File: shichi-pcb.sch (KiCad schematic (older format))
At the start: 34 parts, among them J1 USB_C_Receptacle_HRO_TYPE-C-3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, J2 Conn_01x04_Male, J3 Conn_01x06_Male, J4 Conn_01x04_Male, J5 Conn_01x02_Male, J6 Conn_01x01_Male, SW1 SW_Push, SW2 SW_Push, U1 MCP1700-3302E_SOT23, U2 USBLC6-2SC6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

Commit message: Remove USB headers
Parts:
- removed J2: Conn_01x04_Male, Connector_PinSocket_2.54mm:PinSocket_1x04_P2.54mm_Vertical, symbol Connector:Conn_01x04_Male
- renumbered J3 to J2, J4 to J3, J5 to J4, J6 to J5
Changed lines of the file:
@@
 EESchema Schematic File Version 4
 LIBS:shichi-pcb-cache
-EELAYER 29 0
+EELAYER 30 0
 EELAYER END
 $Descr A4 11693 8268
@@
 NRST
 $Comp
-L power:VCC #PWR04
+L power:VCC #PWR02
 U 1 1 5CFA87A5
 P 2350 4950
-F 0 "#PWR04" H 2350 4800 50  0001 C CNN
+F 0 "#PWR02" H 2350 4800 50  0001 C CNN
 F 1 "VCC" H 2367 5123 50  0000 C CNN
 F 2 "" H 2350 4950 50  0001 C CNN
@@
 $EndComp
 $Comp
-L power:GND #PWR011
+L power:GND #PWR09
 U 1 1 5CFB408D
 P 4300 3250
-F 0 "#PWR011" H 4300 3000 50  0001 C CNN
+F 0 "#PWR09" H 4300 3000 50  0001 C CNN
 F 1 "GND" H 4305 3077 50  0000 C CNN
 F 2 "" H 4300 3250 50  0001 C CNN
@@
 $EndComp
 $Comp
-L power:GND #PWR020
+L power:GND #PWR018
 U 1 1 5CFB6455
 P 7300 1700
-F 0 "#PWR020" H 7300 1450 50  0001 C CNN
+F 0 "#PWR018" H 7300 1450 50  0001 C CNN
 F 1 "GND" H 7305 1527 50  0000 C CNN
 F 2 "" H 7300 1700 50  0001 C CNN
@@
 $EndComp
 $Comp
-L power:GND #PWR027
+L power:GND #PWR025
 U 1 1 5CFB6809
 P 10500 1600
-F 0 "#PWR027" H 10500 1350 50  0001 C CNN
+F 0 "#PWR025" H 10500 1350 50  0001 C CNN
 F 1 "GND" H 10505 1427 50  0000 C CNN
 F 2 "" H 10500 1600 50  0001 C CNN
@@
 	0    -1   -1   0
 $EndComp
-$Comp
-L power:GND #PWR03
-U 1 1 5CFB0CA6
-P 1450 7400
-F 0 "#PWR03" H 1450 7150 50  0001 C CNN
-F 1 "GND" H 1455 7227 50  0000 C CNN
-F 2 "" H 1450 7400 50  0001 C CNN
-F 3 "" H 1450 7400 50  0001 C CNN
-	1    1450 7400
-	0    -1   -1   0
-$EndComp
 Text GLabel 10500 2100 2    50   Input ~ 0
 SCL
@@
 SDA
 $Comp
-L power:GND #PWR029
+L power:GND #PWR027
 U 1 1 5D01D767
 P 10500 2400
-F 0 "#PWR029" H 10500 2150 50  0001 C CNN
+F 0 "#PWR027" H 10500 2150 50  0001 C CNN
 F 1 "GND" H 10505 2227 50  0000 C CNN
 F 2 "" H 10500 2400 50  0001 C CNN
@@
 Wire Wire Line
 	2750 4950 2950 4950
-$Comp
-L power:VCC #PWR02
-U 1 1 5D05176C
-P 1450 7100
-F 0 "#PWR02" H 1450 6950 50  0001 C CNN
-F 1 "VCC" H 1467 7273 50  0000 C CNN
-F 2 "" H 1450 7100 50  0001 C CNN
-F 3 "" H 1450 7100 50  0001 C CNN
-	1    1450 7100
-	0    1    1    0
-$EndComp
 Text GLabel 1950 5550 2    50   Input ~ 0
 D-Bus
@@
 	2200 5150 2350 5150
 $Comp
-L power:GND #PWR05
+L power:GND #PWR03
 U 1 1 5CFAFCDE
 P 2350 5300
-F 0 "#PWR05" H 2350 5050 50  0001 C CNN
+F 0 "#PWR03" H 2350 5050 50  0001 C CNN
 F 1 "GND" H 2355 5127 50  0000 C CNN
 F 2 "" H 2350 5300 50  0001 C CNN
@@
 	4500 6500 4550 6500
 $Comp
-L power:GND #PWR014
+L power:GND #PWR012
 U 1 1 5D32B978
 P 4550 6550
-F 0 "#PWR014" H 4550 6300 50  0001 C CNN
+F 0 "#PWR012" H 4550 6300 50  0001 C CNN
 F 1 "GND" H 4555 6377 50  0000 C CNN
 F 2 "" H 4550 6550 50  0001 C CNN
@@
 	3450 6500 3500 6500
 $Comp
-L power:VCC #PWR08
+L power:VCC #PWR06
 U 1 1 5D31D96D
 P 3450 6450
-F 0 "#PWR08" H 3450 6300 50  0001 C CNN
+F 0 "#PWR06" H 3450 6300 50  0001 C CNN
 F 1 "VCC" H 3467 6623 50  0000 C CNN
 F 2 "" H 3450 6450 50  0001 C CNN
@@
 	4450 5050 4450 5150
 $Comp
-L power:+3.3V #PWR013
+L power:+3.3V #PWR011
 U 1 1 5D1ECA69
 P 4450 4950
-F 0 "#PWR013" H 4450 4800 50  0001 C CNN
+F 0 "#PWR011" H 4450 4800 50  0001 C CNN
 F 1 "+3.3V" H 4465 5123 50  0000 C CNN
 F 2 "" H 4450 4950 50  0001 C CNN
@@
 Connection ~ 4450 5050
 $Comp
-L power:GND #PWR010
+L power:GND #PWR08
 U 1 1 5D1FE5B6
 P 4000 5550
-F 0 "#PWR010" H 4000 5300 50  0001 C CNN
+F 0 "#PWR08" H 4000 5300 50  0001 C CNN
 F 1 "GND" H 4005 5377 50  0000 C CNN
 F 2 "" H 4000 5550 50  0001 C CNN
@@
 $EndComp
 $Comp
-L power:GND #PWR07
+L power:GND #PWR05
 U 1 1 5D281CF4
 P 3350 4050
-F 0 "#PWR07" H 3350 3800 50  0001 C CNN
+F 0 "#PWR05" H 3350 3800 50  0001 C CNN
 F 1 "GND" H 3355 3877 50  0000 C CNN
 F 2 "" H 3350 4050 50  0001 C CNN
@@
 $EndComp
 $Comp
-L power:+3.3V #PWR012
+L power:+3.3V #PWR010
 U 1 1 5D281CFA
 P 4300 3900
-F 0 "#PWR012" H 4300 3750 50  0001 C CNN
+F 0 "#PWR010" H 4300 3750 50  0001 C CNN
 F 1 "+3.3V" H 4315 4073 50  0000 C CNN
 F 2 "" H 4300 3900 50  0001 C CNN
@@
 	6700 1950 7300 1950
 $Comp
-L power:GND #PWR021
+L power:GND #PWR019
 U 1 1 5CFB5A7D
 P 7300 2250
-F 0 "#PWR021" H 7300 2000 50  0001 C CNN
+F 0 "#PWR019" H 7300 2000 50  0001 C CNN
 F 1 "GND" H 7305 2077 50  0000 C CNN
 F 2 "" H 7300 2250 50  0001 C CNN
@@
 $EndComp
 $Comp
-L power:GND #PWR024
+L power:GND #PWR022
 U 1 1 5CFB56F6
 P 7700 2800
-F 0 "#PWR024" H 7700 2550 50  0001 C CNN
+F 0 "#PWR022" H 7700 2550 50  0001 C CNN
 F 1 "GND" H 7705 2627 50  0000 C CNN
 F 2 "" H 7700 2800 50  0001 C CNN
@@
 $EndComp
 $Comp
-L power:GND #PWR022
+L power:GND #PWR020
 U 1 1 5CFB4E50
 P 7300 2800
-F 0 "#PWR022" H 7300 2550 50  0001 C CNN
+F 0 "#PWR020" H 7300 2550 50  0001 C CNN
 F 1 "GND" H 7305 2627 50  0000 C CNN
 F 2 "" H 7300 2800 50  0001 C CNN
@@
 Connection ~ 7300 1400
 $Comp
-L power:GND #PWR023
+L power:GND #PWR021
 U 1 1 5D2D41CB
 P 7700 1700
-F 0 "#PWR023" H 7700 1450 50  0001 C CNN
+F 0 "#PWR021" H 7700 1450 50  0001 C CNN
 F 1 "GND" H 7705 1527 50  0000 C CNN
 F 2 "" H 7700 1700 50  0001 C CNN
@@
 Connection ~ 7700 1400
 $Comp
-L power:GND #PWR025
+L power:GND #PWR023
 U 1 1 5D2DADBD
 P 8100 1700
-F 0 "#PWR025" H 8100 1450 50  0001 C CNN
+F 0 "#PWR023" H 8100 1450 50  0001 C CNN
 F 1 "GND" H 8105 1527 50  0000 C CNN
 F 2 "" H 8100 1700 50  0001 C CNN
@@
 $EndComp
 $Comp
-L power:+3.3V #PWR017
+L power:+3.3V #PWR015
 U 1 1 5D2DDDA7
 P 6500 1400
-F 0 "#PWR017" H 6500 1250 50  0001 C CNN
+F 0 "#PWR015" H 6500 1250 50  0001 C CNN
 F 1 "+3.3V" H 6515 1573 50  0000 C CNN
 F 2 "" H 6500 1400 50  0001 C CNN
@@
 Connection ~ 6500 1400
 $Comp
-L power:+3.3V #PWR018
+L power:+3.3V #PWR016
 U 1 1 5D2DEB65
 P 6700 1950
-F 0 "#PWR018" H 6700 1800 50  0001 C CNN
+F 0 "#PWR016" H 6700 1800 50  0001 C CNN
 F 1 "+3.3V" H 6715 2123 50  0000 C CNN
 F 2 "" H 6700 1950 50  0001 C CNN
@@
 Connection ~ 6700 1950
 $Comp
-L power:+3.3V #PWR019
+L power:+3.3V #PWR017
 U 1 1 5D2DF334
 P 6800 2500
-F 0 "#PWR019" H 6800 2350 50  0001 C CNN
+F 0 "#PWR017" H 6800 2350 50  0001 C CNN
 F 1 "+3.3V" H 6815 2673 50  0000 C CNN
 F 2 "" H 6800 2500 50  0001 C CNN
@@
 SCL
 $Comp
-L power:+3.3V #PWR026
+L power:+3.3V #PWR024
 U 1 1 5D2F0717
 P 10500 1100
-F 0 "#PWR026" H 10500 950 50  0001 C CNN
+F 0 "#PWR024" H 10500 950 50  0001 C CNN
 F 1 "+3.3V" V 10515 1228 50  0000 L CNN
 F 2 "" H 10500 1100 50  0001 C CNN
@@
 SWCLK
 $Comp
-L power:+5V #PWR028
+L power:+5V #PWR026
 U 1 1 5D305D9D
 P 10500 2300
-F 0 "#PWR028" H 10500 2150 50  0001 C CNN
+F 0 "#PWR026" H 10500 2150 50  0001 C CNN
 F 1 "+5V" V 10515 2428 50  0000 L CNN
 F 2 "" H 10500 2300 50  0001 C CNN
@@
 $EndComp
 $Comp
-L power:+5V #PWR06
+L power:+5V #PWR04
 U 1 1 5D30705F
 P 3200 4950
-F 0 "#PWR06" H 3200 4800 50  0001 C CNN
+F 0 "#PWR04" H 3200 4800 50  0001 C CNN
 F 1 "+5V" H 3215 5123 50  0000 C CNN
 F 2 "" H 3200 4950 50  0001 C CNN
@@
 $EndComp
 $Comp
-L power:+5V #PWR09
+L power:+5V #PWR07
 U 1 1 5D30778B
 P 3550 4950
-F 0 "#PWR09" H 3550 4800 50  0001 C CNN
+F 0 "#PWR07" H 3550 4800 50  0001 C CNN
 F 1 "+5V" H 3565 5123 50  0000 C CNN
 F 2 "" H 3550 4950 50  0001 C CNN
@@
 B15
 $Comp
-L power:GND #PWR016
+L power:GND #PWR014
 U 1 1 5D30B602
 P 6400 6250
-F 0 "#PWR016" H 6400 6000 50  0001 C CNN
+F 0 "#PWR014" H 6400 6000 50  0001 C CNN
 F 1 "GND" H 6405 6077 50  0000 C CNN
 F 2 "" H 6400 6250 50  0001 C CNN
@@
 AUDIO_1
 $Comp
-L Connector:Conn_01x02_Male J5
+L Connector:Conn_01x02_Male J4
 U 1 1 5D328A73
 P 10300 2800
-F 0 "J5" H 10408 2981 50  0000 C CNN
+F 0 "J4" H 10408 2981 50  0000 C CNN
 F 1 "Conn_01x02_Male" H 10408 2890 50  0000 C CNN
 F 2 "Connector_PinSocket_2.54mm:PinSocket_1x02_P2.54mm_Vertical" H 10300 2800 50  0001 C CNN
@@
 $EndComp
 $Comp
-L Connector:Conn_01x04_Male J4
+L Connector:Conn_01x04_Male J3
 U 1 1 5D331FB5
 P 10300 2200
-F 0 "J4" H 10408 2481 50  0000 C CNN
+F 0 "J3" H 10408 2481 50  0000 C CNN
 F 1 "Conn_01x04_Male" H 10408 2390 50  0000 C CNN
 F 2 "Connector_PinSocket_2.54mm:PinSocket_1x04_P2.54mm_Vertical" H 10300 2200 50  0001 C CNN
@@
 $EndComp
 $Comp
-L Connector:Conn_01x06_Male J3
+L Connector:Conn_01x06_Male J2
 U 1 1 5D340937
 P 10300 1300
-F 0 "J3" H 10408 1681 50  0000 C CNN
+F 0 "J2" H 10408 1681 50  0000 C CNN
 F 1 "Conn_01x06_Male" H 10408 1590 50  0000 C CNN
 F 2 "Connector_PinSocket_2.54mm:PinSocket_1x06_P2.54mm_Vertical" H 10300 1300 50  0001 C CNN
@@
 $EndComp
 $Comp
-L Connector:Conn_01x01_Male J6
+L Connector:Conn_01x01_Male J5
 U 1 1 5D34E629
 P 10300 3250
-F 0 "J6" H 10408 3431 50  0000 C CNN
+F 0 "J5" H 10408 3431 50  0000 C CNN
 F 1 "Conn_01x01_Male" H 10408 3340 50  0000 C CNN
 F 2 "Connector_PinSocket_2.54mm:PinSocket_1x01_P2.54mm_Vertical" H 10300 3250 50  0001 C CNN
@@
 	5600 7000 5500 7000
 $Comp
-L power:GND #PWR015
+L power:GND #PWR013
 U 1 1 5D361771
 P 5900 7300
-F 0 "#PWR015" H 5900 7050 50  0001 C CNN
+F 0 "#PWR013" H 5900 7050 50  0001 C CNN
 F 1 "GND" H 5905 7127 50  0000 C CNN
 F 2 "" H 5900 7300 50  0001 C CNN
@@
 	5900 7200 6000 7200
 $Comp
-L Connector:Conn_01x04_Male J2
-U 1 1 5D36B1C2
-P 1250 7200
-F 0 "J2" H 1358 7481 50  0000 C CNN
-F 1 "Conn_01x04_Male" H 1358 7390 50  0000 C CNN
-F 2 "Connector_PinSocket_2.54mm:PinSocket_1x04_P2.54mm_Vertical" H 1250 7200 50  0001 C CNN
-F 3 "~" H 1250 7200 50  0001 C CNN
-	1    1250 7200
-	1    0    0    -1
-$EndComp
-Text GLabel 1450 7300 2    50   Input ~ 0
-D+Bus
-Text GLabel 1450 7200 2    50   Input ~ 0
-D-Bus
-$Comp
 L Regulator_Linear:MCP1700-3302E_SOT23 U1

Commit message: Remove B14 and B15 pin headers
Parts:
- removed J4: Conn_01x02_Male, Connector_PinSocket_2.54mm:PinSocket_1x02_P2.54mm_Vertical, symbol Connector:Conn_01x02_Male
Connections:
- net labels removed: B14, B15
- no-connect marks 10 -> 12
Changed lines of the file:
@@
 	1    0    0    -1
 $EndComp
-Text GLabel 5900 5600 0    50   Input ~ 0
-B14
-Text GLabel 5900 5700 0    50   Input ~ 0
-B15
 $Comp
 L power:GND #PWR014
@@
 NoConn ~ 7200 5200
 NoConn ~ 5900 5400
-Text GLabel 10500 2800 2    50   Input ~ 0
-B14
-Text GLabel 10500 2900 2    50   Input ~ 0
-B15
 Text GLabel 10500 3250 2    50   Input ~ 0
 AUDIO_1
-$Comp
-L Connector:Conn_01x02_Male J4
-U 1 1 5D328A73
-P 10300 2800
-F 0 "J4" H 10408 2981 50  0000 C CNN
-F 1 "Conn_01x02_Male" H 10408 2890 50  0000 C CNN
-F 2 "Connector_PinSocket_2.54mm:PinSocket_1x02_P2.54mm_Vertical" H 10300 2800 50  0001 C CNN
-F 3 "~" H 10300 2800 50  0001 C CNN
-	1    10300 2800
-	1    0    0    -1
-$EndComp
 $Comp
 L Connector:Conn_01x04_Male J3
@@
 	1    0    0    -1
 $EndComp
+NoConn ~ 5900 5600
+NoConn ~ 5900 5700
 $EndSCHEMATC

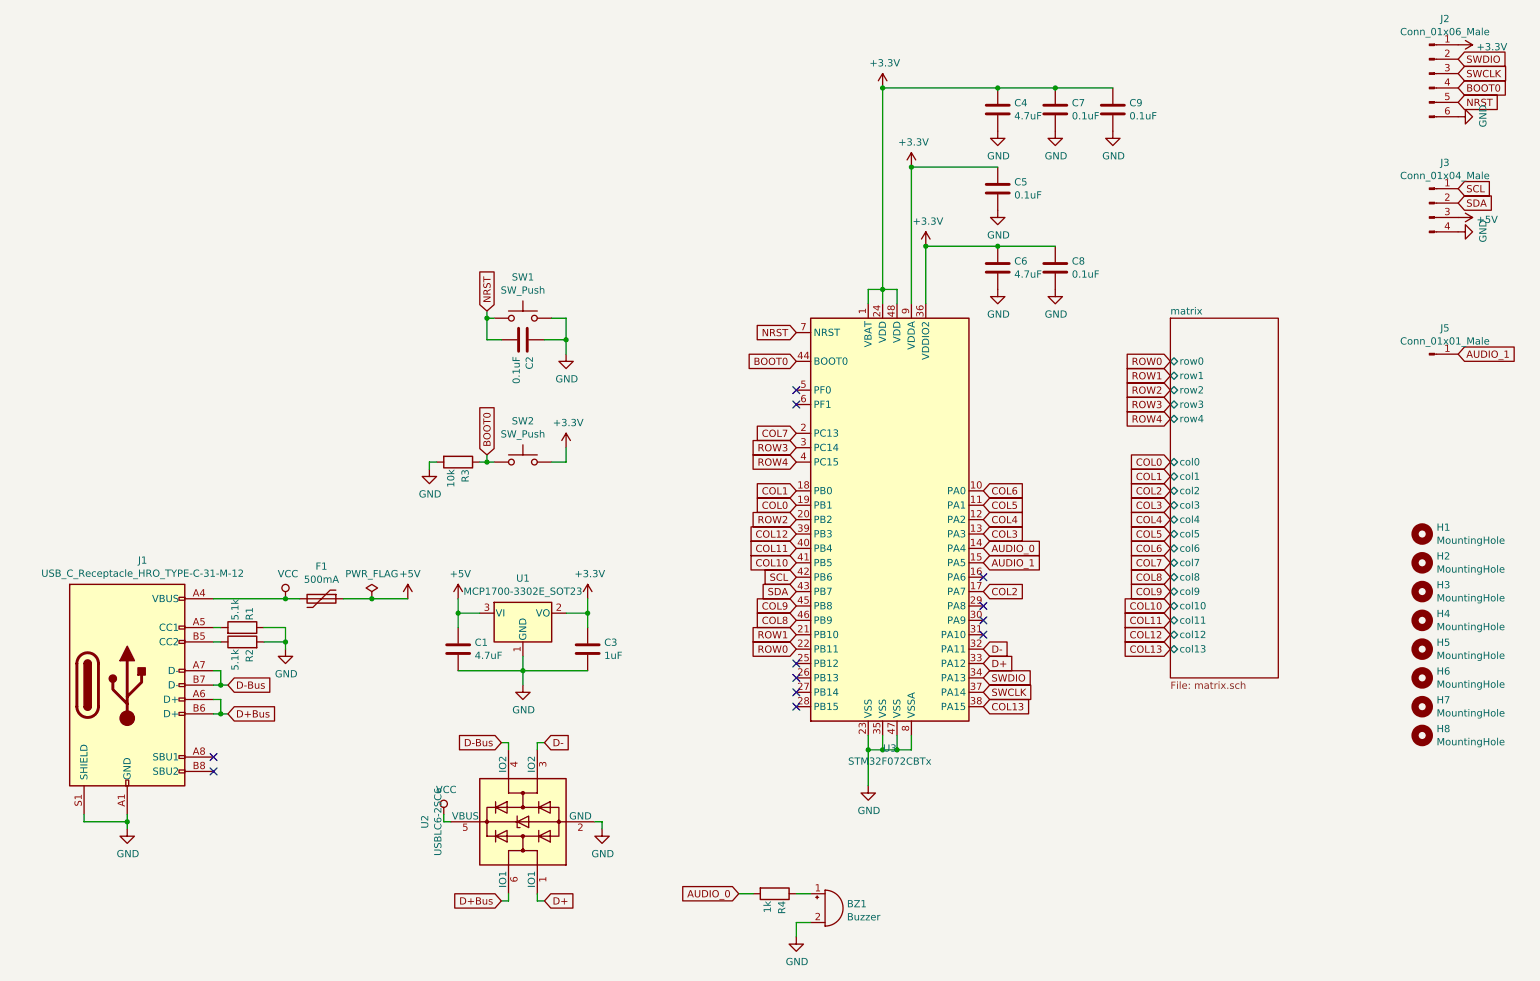
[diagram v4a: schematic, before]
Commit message: Remove AUDIO components
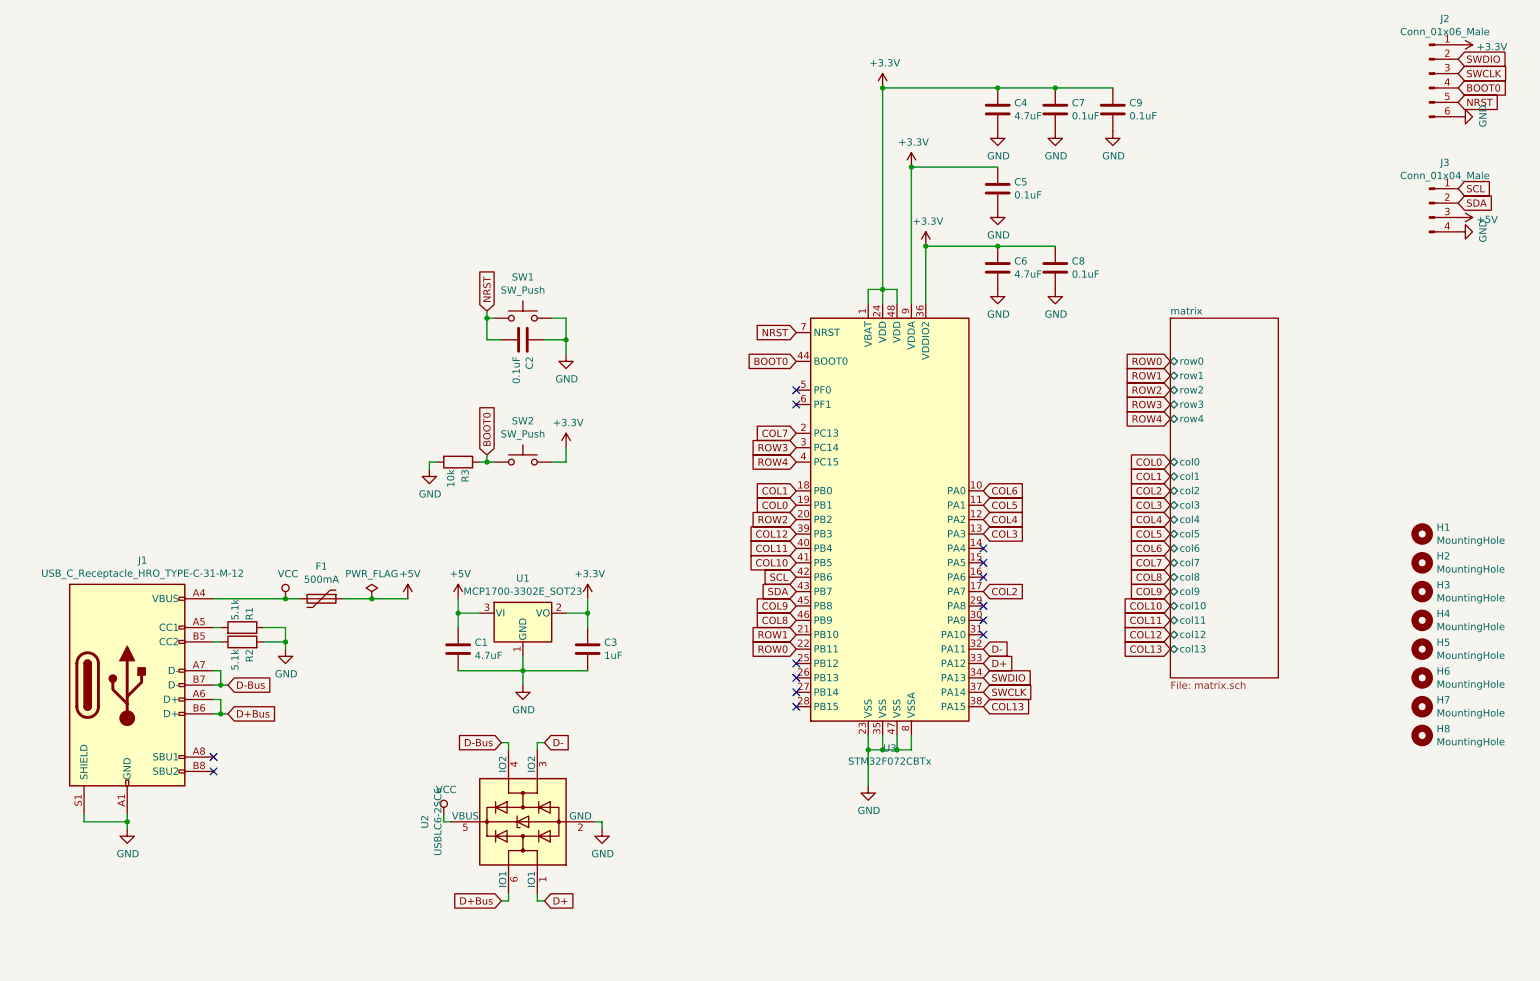
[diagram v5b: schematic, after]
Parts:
- removed BZ1: Buzzer, Buzzer_Beeper:Buzzer_Murata_PKMCS0909E4000-R1, symbol Device:Buzzer
- removed J5: Conn_01x01_Male, Connector_PinSocket_2.54mm:PinSocket_1x01_P2.54mm_Vertical, symbol Connector:Conn_01x01_Male
- removed R4: 1k, Resistor_SMD:R_0805_2012Metric_Pad1.15x1.40mm_HandSolder, symbol Device:R
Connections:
- net AUDIO_0: no longer names the net of U3.14 (PA4)
- net AUDIO_1: no longer names the net of U3.15 (PA5)
- no-connect marks 12 -> 14
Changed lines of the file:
@@
 $EndComp
 $Comp
-L power:GND #PWR018
+L power:GND #PWR017
 U 1 1 5CFB6455
 P 7300 1700
-F 0 "#PWR018" H 7300 1450 50  0001 C CNN
+F 0 "#PWR017" H 7300 1450 50  0001 C CNN
 F 1 "GND" H 7305 1527 50  0000 C CNN
 F 2 "" H 7300 1700 50  0001 C CNN
@@
 $EndComp
 $Comp
-L power:GND #PWR025
+L power:GND #PWR024
 U 1 1 5CFB6809
 P 10500 1600
-F 0 "#PWR025" H 10500 1350 50  0001 C CNN
+F 0 "#PWR024" H 10500 1350 50  0001 C CNN
 F 1 "GND" H 10505 1427 50  0000 C CNN
 F 2 "" H 10500 1600 50  0001 C CNN
@@
 SDA
 $Comp
-L power:GND #PWR027
+L power:GND #PWR026
 U 1 1 5D01D767
 P 10500 2400
-F 0 "#PWR027" H 10500 2150 50  0001 C CNN
+F 0 "#PWR026" H 10500 2150 50  0001 C CNN
 F 1 "GND" H 10505 2227 50  0000 C CNN
 F 2 "" H 10500 2400 50  0001 C CNN
@@
 	6700 1950 7300 1950
 $Comp
-L power:GND #PWR019
+L power:GND #PWR018
 U 1 1 5CFB5A7D
 P 7300 2250
-F 0 "#PWR019" H 7300 2000 50  0001 C CNN
+F 0 "#PWR018" H 7300 2000 50  0001 C CNN
 F 1 "GND" H 7305 2077 50  0000 C CNN
 F 2 "" H 7300 2250 50  0001 C CNN
@@
 $EndComp
 $Comp
-L power:GND #PWR022
+L power:GND #PWR021
 U 1 1 5CFB56F6
 P 7700 2800
-F 0 "#PWR022" H 7700 2550 50  0001 C CNN
+F 0 "#PWR021" H 7700 2550 50  0001 C CNN
 F 1 "GND" H 7705 2627 50  0000 C CNN
 F 2 "" H 7700 2800 50  0001 C CNN
@@
 $EndComp
 $Comp
-L power:GND #PWR020
+L power:GND #PWR019
 U 1 1 5CFB4E50
 P 7300 2800
-F 0 "#PWR020" H 7300 2550 50  0001 C CNN
+F 0 "#PWR019" H 7300 2550 50  0001 C CNN
 F 1 "GND" H 7305 2627 50  0000 C CNN
 F 2 "" H 7300 2800 50  0001 C CNN
@@
 Connection ~ 7300 1400
 $Comp
-L power:GND #PWR021
+L power:GND #PWR020
 U 1 1 5D2D41CB
 P 7700 1700
-F 0 "#PWR021" H 7700 1450 50  0001 C CNN
+F 0 "#PWR020" H 7700 1450 50  0001 C CNN
 F 1 "GND" H 7705 1527 50  0000 C CNN
 F 2 "" H 7700 1700 50  0001 C CNN
@@
 Connection ~ 7700 1400
 $Comp
-L power:GND #PWR023
+L power:GND #PWR022
 U 1 1 5D2DADBD
 P 8100 1700
-F 0 "#PWR023" H 8100 1450 50  0001 C CNN
+F 0 "#PWR022" H 8100 1450 50  0001 C CNN
 F 1 "GND" H 8105 1527 50  0000 C CNN
 F 2 "" H 8100 1700 50  0001 C CNN
@@
 $EndComp
 $Comp
-L power:+3.3V #PWR015
+L power:+3.3V #PWR014
 U 1 1 5D2DDDA7
 P 6500 1400
-F 0 "#PWR015" H 6500 1250 50  0001 C CNN
+F 0 "#PWR014" H 6500 1250 50  0001 C CNN
 F 1 "+3.3V" H 6515 1573 50  0000 C CNN
 F 2 "" H 6500 1400 50  0001 C CNN
@@
 Connection ~ 6500 1400
 $Comp
-L power:+3.3V #PWR016
+L power:+3.3V #PWR015
 U 1 1 5D2DEB65
 P 6700 1950
-F 0 "#PWR016" H 6700 1800 50  0001 C CNN
+F 0 "#PWR015" H 6700 1800 50  0001 C CNN
 F 1 "+3.3V" H 6715 2123 50  0000 C CNN
 F 2 "" H 6700 1950 50  0001 C CNN
@@
 Connection ~ 6700 1950
 $Comp
-L power:+3.3V #PWR017
+L power:+3.3V #PWR016
 U 1 1 5D2DF334
 P 6800 2500
-F 0 "#PWR017" H 6800 2350 50  0001 C CNN
+F 0 "#PWR016" H 6800 2350 50  0001 C CNN
 F 1 "+3.3V" H 6815 2673 50  0000 C CNN
 F 2 "" H 6800 2500 50  0001 C CNN
@@
 Text GLabel 7200 5400 2    50   Input ~ 0
 D+
-Text GLabel 7200 4600 2    50   Input ~ 0
-AUDIO_0
-Text GLabel 7200 4700 2    50   Input ~ 0
-AUDIO_1
 Text GLabel 8500 3300 0    50   Input ~ 0
 ROW0
@@
 SCL
 $Comp
-L power:+3.3V #PWR024
+L power:+3.3V #PWR023
 U 1 1 5D2F0717
 P 10500 1100
-F 0 "#PWR024" H 10500 950 50  0001 C CNN
+F 0 "#PWR023" H 10500 950 50  0001 C CNN
 F 1 "+3.3V" V 10515 1228 50  0000 L CNN
 F 2 "" H 10500 1100 50  0001 C CNN
@@
 SWCLK
 $Comp
-L power:+5V #PWR026
+L power:+5V #PWR025
 U 1 1 5D305D9D
 P 10500 2300
-F 0 "#PWR026" H 10500 2150 50  0001 C CNN
+F 0 "#PWR025" H 10500 2150 50  0001 C CNN
 F 1 "+5V" V 10515 2428 50  0000 L CNN
 F 2 "" H 10500 2300 50  0001 C CNN
@@
 $EndComp
 $Comp
-L power:GND #PWR014
+L power:GND #PWR013
 U 1 1 5D30B602
 P 6400 6250
-F 0 "#PWR014" H 6400 6000 50  0001 C CNN
+F 0 "#PWR013" H 6400 6000 50  0001 C CNN
 F 1 "GND" H 6405 6077 50  0000 C CNN
 F 2 "" H 6400 6250 50  0001 C CNN
@@
 NoConn ~ 7200 5200
 NoConn ~ 5900 5400
-Text GLabel 10500 3250 2    50   Input ~ 0
-AUDIO_1
 $Comp
 L Connector:Conn_01x04_Male J3
@@
 $EndComp
 $Comp
-L Connector:Conn_01x01_Male J5
-U 1 1 5D34E629
-P 10300 3250
-F 0 "J5" H 10408 3431 50  0000 C CNN
-F 1 "Conn_01x01_Male" H 10408 3340 50  0000 C CNN
-F 2 "Connector_PinSocket_2.54mm:PinSocket_1x01_P2.54mm_Vertical" H 10300 3250 50  0001 C CNN
-F 3 "~" H 10300 3250 50  0001 C CNN
-	1    10300 3250
-	1    0    0    -1
-$EndComp
-$Comp
-L Device:Buzzer BZ1
-U 1 1 5D352016
-P 6100 7100
-F 0 "BZ1" H 6252 7129 50  0000 L CNN
-F 1 "Buzzer" H 6252 7038 50  0000 L CNN
-F 2 "Buzzer_Beeper:Buzzer_Murata_PKMCS0909E4000-R1" V 6075 7200 50  0001 C CNN
-F 3 "~" V 6075 7200 50  0001 C CNN
-	1    6100 7100
-	1    0    0    -1
-$EndComp
-Text GLabel 5500 7000 0    50   Input ~ 0
-AUDIO_0
-$Comp
-L Device:R R4
-U 1 1 5D35C35E
-P 5750 7000
-F 0 "R4" H 5800 7050 50  0000 L CNN
-F 1 "1k" H 5800 6950 50  0000 L CNN
-F 2 "Resistor_SMD:R_0805_2012Metric_Pad1.15x1.40mm_HandSolder" V 5680 7000 50  0001 C CNN
-F 3 "~" H 5750 7000 50  0001 C CNN
-	1    5750 7000
-	0    1    1    0
-$EndComp
-Wire Wire Line
-	5900 7000 6000 7000
-Wire Wire Line
-	5600 7000 5500 7000
-$Comp
-L power:GND #PWR013
-U 1 1 5D361771
-P 5900 7300
-F 0 "#PWR013" H 5900 7050 50  0001 C CNN
-F 1 "GND" H 5905 7127 50  0000 C CNN
-F 2 "" H 5900 7300 50  0001 C CNN
-F 3 "" H 5900 7300 50  0001 C CNN
-	1    5900 7300
-	1    0    0    -1
-$EndComp
-Wire Wire Line
-	5900 7300 5900 7200
-Wire Wire Line
-	5900 7200 6000 7200
-$Comp
 L Regulator_Linear:MCP1700-3302E_SOT23 U1
 U 1 1 5D1F289F
@@
 NoConn ~ 5900 5600
 NoConn ~ 5900 5700
+NoConn ~ 7200 4600
+NoConn ~ 7200 4700
 $EndSCHEMATC
